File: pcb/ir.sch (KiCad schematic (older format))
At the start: 2 parts, among them Q1 AO3400

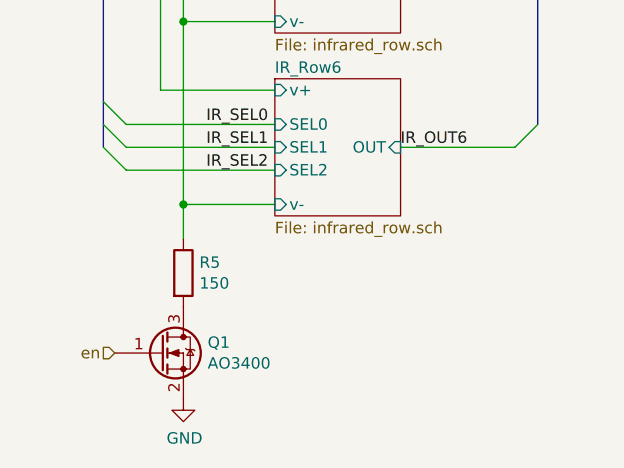
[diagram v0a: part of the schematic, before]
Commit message: Resistor value corrected
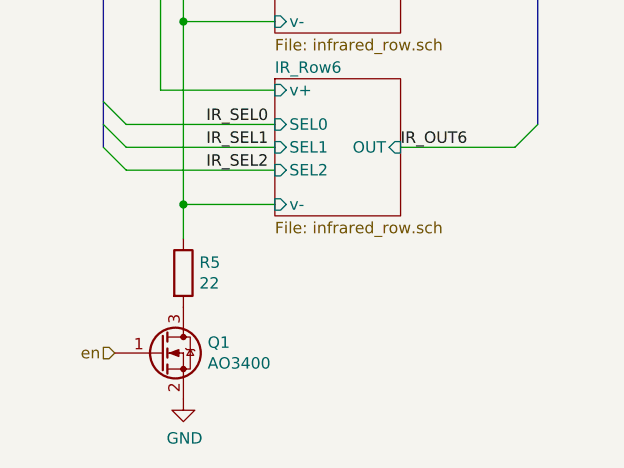
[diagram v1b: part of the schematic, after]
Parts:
- R5: value 150 -> 22
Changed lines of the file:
@@
 P 5300 6700
 F 0 "R5" H 5370 6746 50  0000 L CNN
-F 1 "150" H 5370 6655 50  0000 L CNN
+F 1 "22" H 5370 6655 50  0000 L CNN
 F 2 "" V 5230 6700 50  0001 C CNN
 F 3 "~" H 5300 6700 50  0001 C CNN

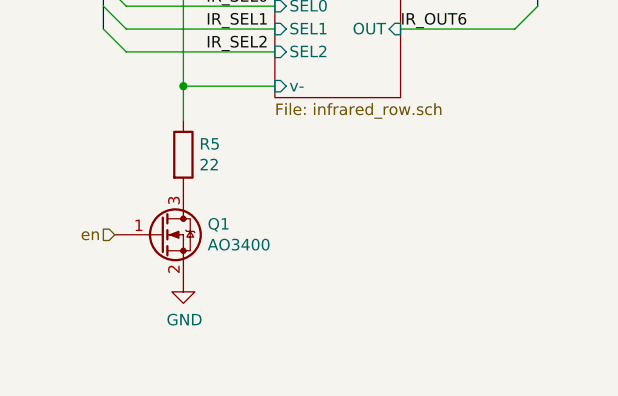
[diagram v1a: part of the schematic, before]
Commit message: Added 0 ohm resistor to power switch
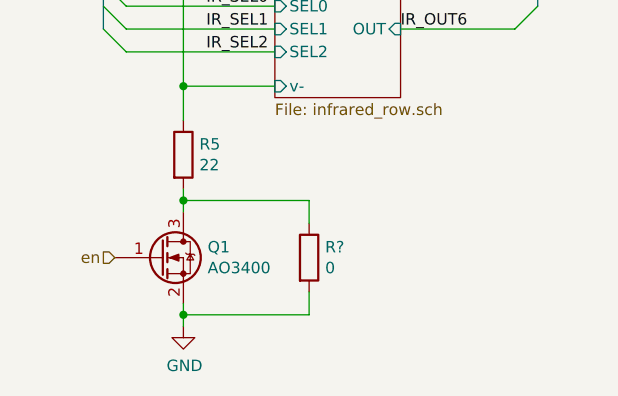
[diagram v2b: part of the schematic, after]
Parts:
- added R?: 0, symbol Device:R
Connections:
- net GND: now also R?.2
- net at Q1.3 (D), R5.2: now also R?.1
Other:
- moved on the sheet: Q1
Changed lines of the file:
@@
 L power:GND #PWR0102
 U 1 1 5D41F6C3
-P 5300 7250
-F 0 "#PWR0102" H 5300 7000 50  0001 C CNN
-F 1 "GND" H 5305 7077 50  0000 C CNN
-F 2 "" H 5300 7250 50  0001 C CNN
-F 3 "" H 5300 7250 50  0001 C CNN
-	1    5300 7250
+P 5300 7450
+F 0 "#PWR0102" H 5300 7200 50  0001 C CNN
+F 1 "GND" H 5305 7277 50  0000 C CNN
+F 2 "" H 5300 7450 50  0001 C CNN
+F 3 "" H 5300 7450 50  0001 C CNN
+	1    5300 7450
 	1    0    0    -1
 $EndComp
@@
 Wire Wire Line
 	5300 4800 5300 4000
-Text HLabel 5000 7050 0    50   Input ~ 0
+Text HLabel 5000 7150 0    50   Input ~ 0
 en
 $Sheet
@@
 L rasbot:AO3400 Q1
 U 1 1 5D362773
-P 5250 7050
-F 0 "Q1" H 5406 7096 50  0000 L CNN
-F 1 "AO3400" H 5406 7005 50  0000 L CNN
-F 2 "Package_TO_SOT_SMD:SOT-23" H 5975 6975 50  0001 C CNN
-F 3 "http://dalincom.ru/datasheet/AO3400.pdf" H 5250 7050 50  0001 C CNN
-	1    5250 7050
+P 5250 7150
+F 0 "Q1" H 5406 7196 50  0000 L CNN
+F 1 "AO3400" H 5406 7105 50  0000 L CNN
+F 2 "Package_TO_SOT_SMD:SOT-23" H 5975 7075 50  0001 C CNN
+F 3 "http://dalincom.ru/datasheet/AO3400.pdf" H 5250 7150 50  0001 C CNN
+	1    5250 7150
 	1    0    0    -1
 $EndComp
@@
 Connection ~ 5200 1900
 Connection ~ 5200 1100
+Wire Wire Line
+	5300 6950 5300 6900
+$Comp
+L Device:R R?
+U 1 1 5D3ABC64
+P 5850 7150
+F 0 "R?" H 5920 7196 50  0000 L CNN
+F 1 "0" H 5920 7105 50  0000 L CNN
+F 2 "" V 5780 7150 50  0001 C CNN
+F 3 "~" H 5850 7150 50  0001 C CNN
+	1    5850 7150
+	1    0    0    -1
+$EndComp
+Wire Wire Line
+	5300 7450 5300 7400
+Wire Wire Line
+	5850 7300 5850 7400
+Wire Wire Line
+	5850 7400 5300 7400
+Connection ~ 5300 7400
+Wire Wire Line
+	5300 7400 5300 7350
+Wire Wire Line
+	5850 7000 5850 6900
+Wire Wire Line
+	5850 6900 5300 6900
 Wire Bus Line
 	6850 1000 6850 6050
 Wire Bus Line
 	4950 1000 4950 6150
+Connection ~ 5300 6900
+Wire Wire Line
+	5300 6900 5300 6850
 $EndSCHEMATC

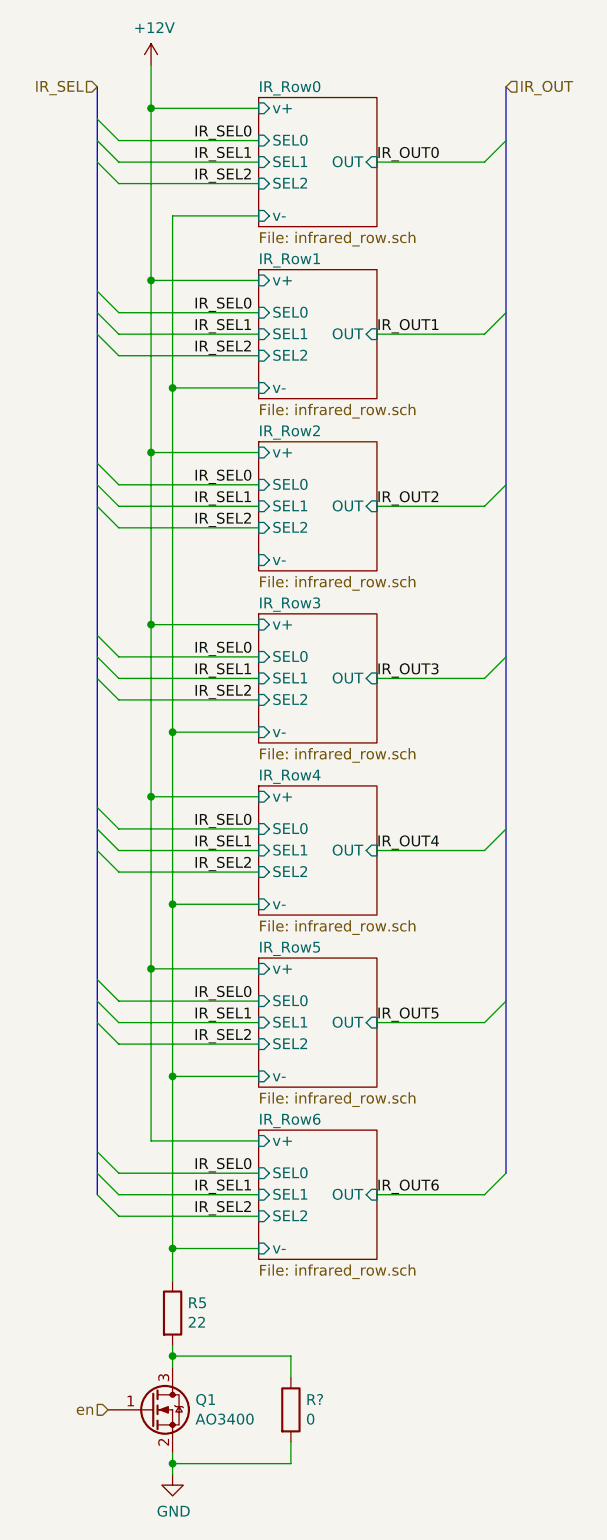
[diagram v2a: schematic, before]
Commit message: Fix IR Sensors
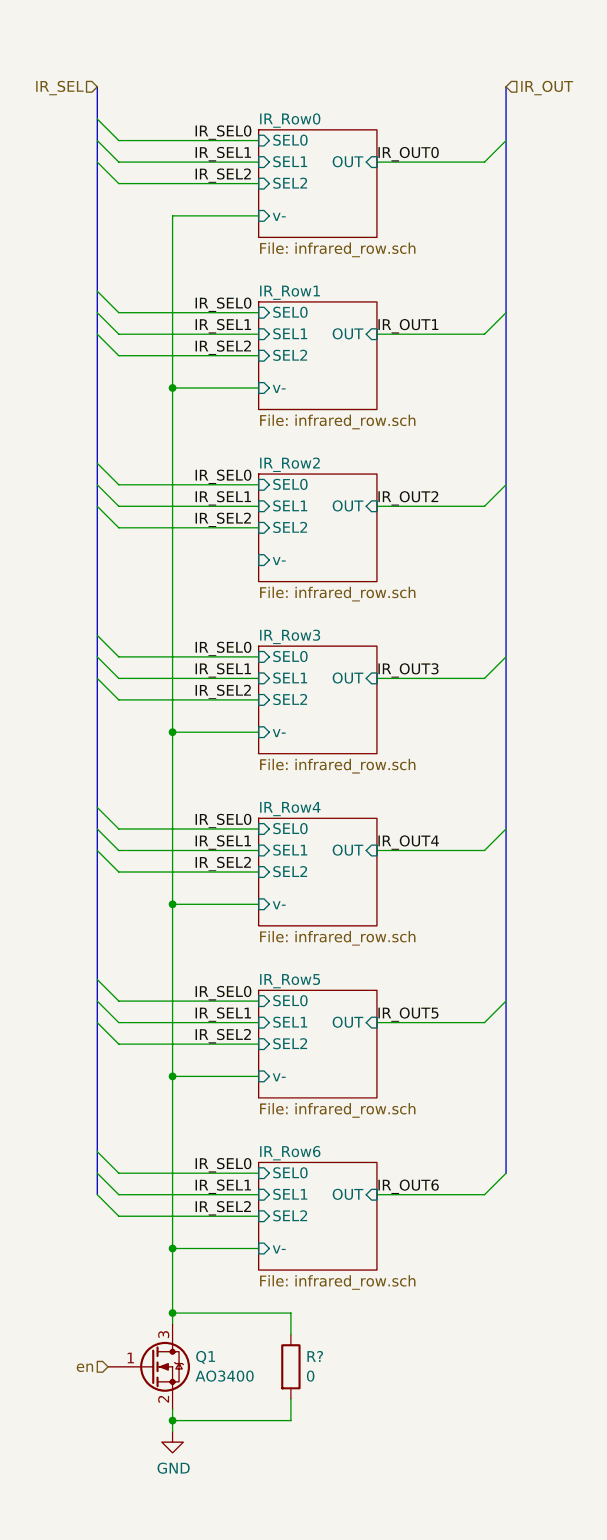
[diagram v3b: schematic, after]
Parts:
- removed R5: 22, symbol Device:R
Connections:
- net IR_Row0/v-: now also Q1.3 (D), R?.1
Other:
- moved on the sheet: Q1, R?
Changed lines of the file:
@@
 $EndDescr
 $Sheet
-S 5700 1050 550  600
+S 5700 1200 550  500
 U 5D254F86
 F0 "IR_Row0" 50
@@
 F3 "SEL1" I L 5700 1350 50
 F4 "SEL2" I L 5700 1450 50
-F5 "v+" I L 5700 1100 50
 F6 "v-" I L 5700 1600 50
 F7 "OUT" I R 6250 1350 50
@@
 Wire Wire Line
 	5050 1450 5700 1450
-$Comp
-L power:+12V #PWR0101
-U 1 1 5D40BFEA
-P 5200 900
-F 0 "#PWR0101" H 5200 750 50  0001 C CNN
-F 1 "+12V" H 5215 1073 50  0000 C CNN
-F 2 "" H 5200 900 50  0001 C CNN
-F 3 "" H 5200 900 50  0001 C CNN
-	1    5200 900
-	1    0    0    -1
-$EndComp
-Wire Wire Line
-	5200 900  5200 1100
-$Sheet
-S 5700 1850 550  600
+$Sheet
+S 5700 2000 550  500
 U 5D40D6FB
 F0 "IR_Row1" 50
@@
 F3 "SEL1" I L 5700 2150 50
 F4 "SEL2" I L 5700 2250 50
-F5 "v+" I L 5700 1900 50
 F6 "v-" I L 5700 2400 50
 F7 "OUT" I R 6250 2150 50
 $EndSheet
 $Sheet
-S 5700 3450 550  600
+S 5700 3600 550  500
 U 5D40DB29
 F0 "IR_Row3" 50
@@
 F3 "SEL1" I L 5700 3750 50
 F4 "SEL2" I L 5700 3850 50
-F5 "v+" I L 5700 3500 50
 F6 "v-" I L 5700 4000 50
 F7 "OUT" I R 6250 3750 50
 $EndSheet
 $Sheet
-S 5700 4250 550  600
+S 5700 4400 550  500
 U 5D40DC5E
 F0 "IR_Row4" 50
@@
 F3 "SEL1" I L 5700 4550 50
 F4 "SEL2" I L 5700 4650 50
-F5 "v+" I L 5700 4300 50
 F6 "v-" I L 5700 4800 50
 F7 "OUT" I R 6250 4550 50
 $EndSheet
 $Sheet
-S 5700 5050 550  600
+S 5700 5200 550  500
 U 5D40DD62
 F0 "IR_Row5" 50
@@
 F3 "SEL1" I L 5700 5350 50
 F4 "SEL2" I L 5700 5450 50
-F5 "v+" I L 5700 5100 50
 F6 "v-" I L 5700 5600 50
 F7 "OUT" I R 6250 5350 50
 $EndSheet
-$Sheet
-S 5700 5850 550  600
-U 5D40E002
-F0 "IR_Row6" 50
-F1 "infrared_row.sch" 50
-F2 "SEL0" I L 5700 6050 50
-F3 "SEL1" I L 5700 6150 50
-F4 "SEL2" I L 5700 6250 50
-F5 "v+" I L 5700 5900 50
-F6 "v-" I L 5700 6400 50
-F7 "OUT" I R 6250 6150 50
-$EndSheet
-Wire Wire Line
-	5700 1100 5200 1100
-Wire Wire Line
-	5700 1900 5200 1900
-Wire Wire Line
-	5200 1900 5200 2700
-Wire Wire Line
-	5700 2700 5200 2700
-Connection ~ 5200 2700
-Wire Wire Line
-	5200 2700 5200 3500
-Wire Wire Line
-	5700 3500 5200 3500
-Connection ~ 5200 3500
-Wire Wire Line
-	5200 3500 5200 4300
-Wire Wire Line
-	5700 4300 5200 4300
-Connection ~ 5200 4300
-Wire Wire Line
-	5200 4300 5200 5100
-Wire Wire Line
-	5700 5100 5200 5100
-Connection ~ 5200 5100
-Wire Wire Line
-	5700 5900 5200 5900
-Wire Wire Line
-	5200 5100 5200 5900
 Entry Wire Line
 	6750 6150 6850 6050
@@
 IR_OUT6
 $Comp
-L Device:R R5
-U 1 1 5D41D265
-P 5300 6700
-F 0 "R5" H 5370 6746 50  0000 L CNN
-F 1 "22" H 5370 6655 50  0000 L CNN
-F 2 "" V 5230 6700 50  0001 C CNN
-F 3 "~" H 5300 6700 50  0001 C CNN
-	1    5300 6700
+L power:GND #PWR0102
+U 1 1 5D41F6C3
+P 5300 7250
+F 0 "#PWR0102" H 5300 7000 50  0001 C CNN
+F 1 "GND" H 5305 7077 50  0000 C CNN
+F 2 "" H 5300 7250 50  0001 C CNN
+F 3 "" H 5300 7250 50  0001 C CNN
+	1    5300 7250
 	1    0    0    -1
 $EndComp
-$Comp
-L power:GND #PWR0102
-U 1 1 5D41F6C3
-P 5300 7450
-F 0 "#PWR0102" H 5300 7200 50  0001 C CNN
-F 1 "GND" H 5305 7277 50  0000 C CNN
-F 2 "" H 5300 7450 50  0001 C CNN
-F 3 "" H 5300 7450 50  0001 C CNN
-	1    5300 7450
-	1    0    0    -1
-$EndComp
-Wire Wire Line
-	5300 6550 5300 6400
-Wire Wire Line
-	5300 6400 5700 6400
-Wire Wire Line
-	5300 6400 5300 5600
-Wire Wire Line
-	5300 5600 5700 5600
-Connection ~ 5300 6400
-Wire Wire Line
-	5300 5600 5300 4800
-Wire Wire Line
-	5300 1600 5700 1600
-Connection ~ 5300 5600
-Wire Wire Line
-	5700 2400 5300 2400
-Connection ~ 5300 2400
-Wire Wire Line
-	5300 2400 5300 1600
-Wire Wire Line
-	5700 4000 5300 4000
-Connection ~ 5300 4000
-Wire Wire Line
-	5300 4000 5300 2400
-Wire Wire Line
-	5700 4800 5300 4800
-Connection ~ 5300 4800
-Wire Wire Line
-	5300 4800 5300 4000
-Text HLabel 5000 7150 0    50   Input ~ 0
+Text HLabel 5000 6950 0    50   Input ~ 0
 en
 $Sheet
-S 5700 2650 550  600
+S 5700 2800 550  500
 U 5D40DA1E
 F0 "IR_Row2" 50
@@
 F3 "SEL1" I L 5700 2950 50
 F4 "SEL2" I L 5700 3050 50
-F5 "v+" I L 5700 2700 50
 F6 "v-" I L 5700 3200 50
 F7 "OUT" I R 6250 2950 50
@@
 L rasbot:AO3400 Q1
 U 1 1 5D362773
-P 5250 7150
-F 0 "Q1" H 5406 7196 50  0000 L CNN
-F 1 "AO3400" H 5406 7105 50  0000 L CNN
-F 2 "Package_TO_SOT_SMD:SOT-23" H 5975 7075 50  0001 C CNN
-F 3 "http://dalincom.ru/datasheet/AO3400.pdf" H 5250 7150 50  0001 C CNN
-	1    5250 7150
+P 5250 6950
+F 0 "Q1" H 5406 6996 50  0000 L CNN
+F 1 "AO3400" H 5406 6905 50  0000 L CNN
+F 2 "Package_TO_SOT_SMD:SOT-23" H 5975 6875 50  0001 C CNN
+F 3 "http://dalincom.ru/datasheet/AO3400.pdf" H 5250 6950 50  0001 C CNN
+	1    5250 6950
 	1    0    0    -1
 $EndComp
 Wire Wire Line
-	5200 1900 5200 1100
-Connection ~ 5200 1900
-Connection ~ 5200 1100
-Wire Wire Line
-	5300 6950 5300 6900
+	5300 6750 5300 6700
 $Comp
 L Device:R R?
 U 1 1 5D3ABC64
-P 5850 7150
-F 0 "R?" H 5920 7196 50  0000 L CNN
-F 1 "0" H 5920 7105 50  0000 L CNN
-F 2 "" V 5780 7150 50  0001 C CNN
-F 3 "~" H 5850 7150 50  0001 C CNN
-	1    5850 7150
+P 5850 6950
+F 0 "R?" H 5920 6996 50  0000 L CNN
+F 1 "0" H 5920 6905 50  0000 L CNN
+F 2 "" V 5780 6950 50  0001 C CNN
+F 3 "~" H 5850 6950 50  0001 C CNN
+	1    5850 6950
 	1    0    0    -1
 $EndComp
 Wire Wire Line
-	5300 7450 5300 7400
-Wire Wire Line
-	5850 7300 5850 7400
-Wire Wire Line
-	5850 7400 5300 7400
-Connection ~ 5300 7400
-Wire Wire Line
-	5300 7400 5300 7350
-Wire Wire Line
-	5850 7000 5850 6900
-Wire Wire Line
-	5850 6900 5300 6900
+	5300 7250 5300 7200
+Wire Wire Line
+	5850 7100 5850 7200
+Wire Wire Line
+	5850 7200 5300 7200
+Connection ~ 5300 7200
+Wire Wire Line
+	5300 7200 5300 7150
+Wire Wire Line
+	5850 6800 5850 6700
+Wire Wire Line
+	5850 6700 5300 6700
+Connection ~ 5300 6700
+Wire Wire Line
+	5300 6400 5700 6400
+Wire Wire Line
+	5300 6400 5300 5600
+Wire Wire Line
+	5300 5600 5700 5600
+Connection ~ 5300 5600
+Wire Wire Line
+	5300 5600 5300 4800
+Wire Wire Line
+	5700 4800 5300 4800
+Connection ~ 5300 4800
+Wire Wire Line
+	5300 4800 5300 4000
+Wire Wire Line
+	5700 4000 5300 4000
+Connection ~ 5300 4000
+Wire Wire Line
+	5300 4000 5300 2400
+Wire Wire Line
+	5700 2400 5300 2400
+Wire Wire Line
+	5300 1600 5700 1600
+Connection ~ 5300 2400
+Wire Wire Line
+	5300 2400 5300 1600
+$Sheet
+S 5700 6000 550  500
+U 5D40E002
+F0 "IR_Row6" 50
+F1 "infrared_row.sch" 50
+F2 "SEL0" I L 5700 6050 50
+F3 "SEL1" I L 5700 6150 50
+F4 "SEL2" I L 5700 6250 50
+F6 "v-" I L 5700 6400 50
+F7 "OUT" I R 6250 6150 50
+$EndSheet
+Wire Wire Line
+	5300 6400 5300 6700
 Wire Bus Line
 	6850 1000 6850 6050
 Wire Bus Line
 	4950 1000 4950 6150
-Connection ~ 5300 6900
-Wire Wire Line
-	5300 6900 5300 6850
+Connection ~ 5300 6400
 $EndSCHEMATC
